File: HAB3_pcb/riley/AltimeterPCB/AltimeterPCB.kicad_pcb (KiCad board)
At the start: 2 copper layers, 4 parts, among them J1 Conn_01x04_Female, J2 Conn_02x01, U1 MS560702BA03-00

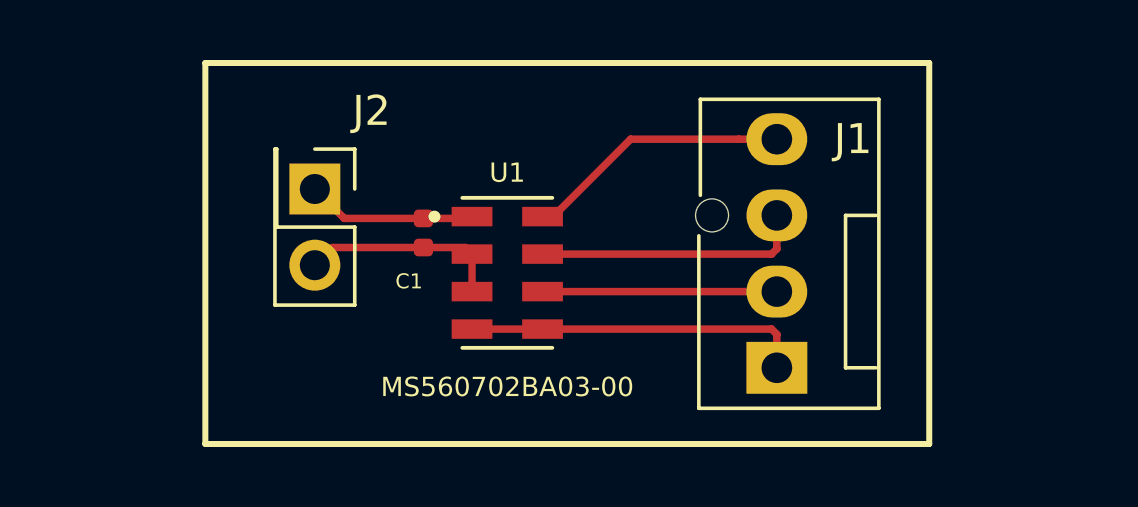
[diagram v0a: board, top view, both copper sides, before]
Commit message: updated labels on riley's pcb
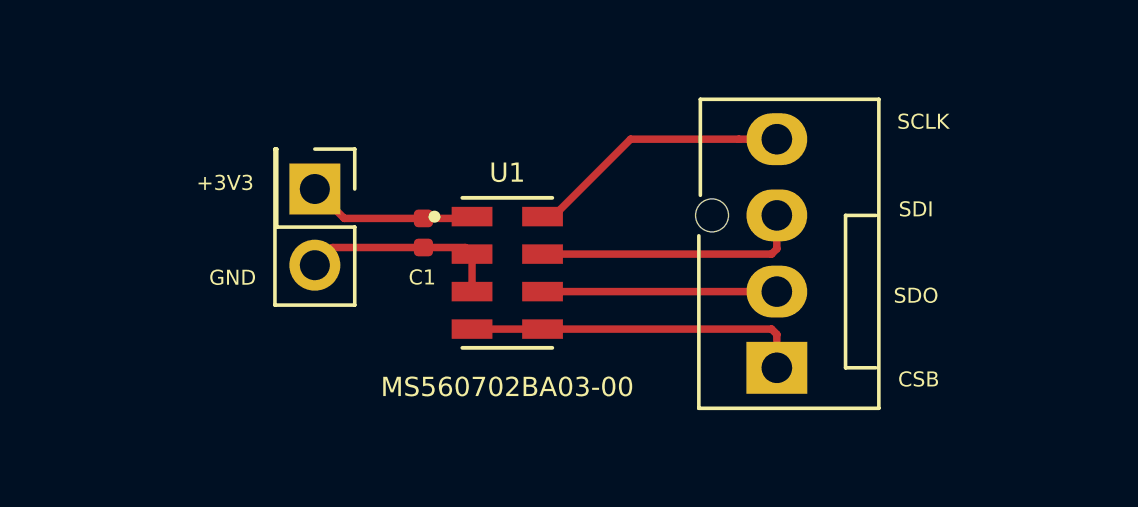
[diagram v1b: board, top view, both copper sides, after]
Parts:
- ?: renamed from J1; value Conn_01x04_Female -> (none)
- ?: renamed from J2; value Conn_02x01 -> (none)
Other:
- copper layers 2 -> 4
- board text added: "+3V3"
- board text added: "CSB"
- board text added: "GND"
- board text added: "SCLK"
- board text added: "SDI"
- board text added: "SDO"
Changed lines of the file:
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@@
   (layers
     (0 F.Cu signal)
+    (1 In1.Cu power)
+    (2 In2.Cu power)
     (31 B.Cu signal)
     (32 B.Adhes user)
@@
     (descr "4-pin CPU fan Through hole pin header, e.g. for Wieson part number 2366C888-007 Molex 47053-1000, Foxconn HF27040-M1, Tyco 1470947-1 or equivalent, see http://www.formfactors.org/developer%5Cspecs%5Crev1_2_public.pdf")
     (tags "pin header 4-pin CPU fan")
-    (fp_text reference J1 (at 7.62 2.54) (layer F.SilkS)
-      (effects (font (size 1 1) (thickness 0.15)))
-    )
-    (fp_text value Conn_01x04_Female (at 3.83 4.21 90) (layer F.Fab)
+    (fp_text reference "" (at 5.91 2.06) (layer F.SilkS) hide
+      (effects (font (size 1 1) (thickness 0.15)))
+    )
+    (fp_text value "" (at 3.83 4.21 90) (layer F.Fab) hide
       (effects (font (size 0.5 0.5) (thickness 0.125)))
     )
@@
     (tags capacitor)
     (attr smd)
-    (fp_text reference C1 (at 1.615 0.48) (layer F.SilkS)
+    (fp_text reference C1 (at 1.485 0.04) (layer F.SilkS)
       (effects (font (size 0.5 0.5) (thickness 0.125)))
     )
@@
     (descr "Through hole straight pin header, 2x01, 2.54mm pitch, double rows")
     (tags "Through hole pin header THT 2x01 2.54mm double row")
-    (fp_text reference J2 (at -2.6 -1.89) (layer F.SilkS)
-      (effects (font (size 1 1) (thickness 0.15)))
-    )
-    (fp_text value Conn_02x01 (at 1.25 2.57 270) (layer F.Fab)
+    (fp_text reference "" (at -2.6 -1.89) (layer F.SilkS) hide
+      (effects (font (size 1 1) (thickness 0.15)))
+    )
+    (fp_text value "" (at 1.25 2.57 270) (layer F.Fab)
       (effects (font (size 1 1) (thickness 0.15)))
     )
@@
     )
   )
-  (gr_line (start 116.84 109.22) (end 124.46 109.22) (layer F.SilkS) (width 0.2))
-  (gr_line (start 116.84 96.52) (end 116.84 109.22) (layer F.SilkS) (width 0.2))
-  (gr_line (start 124.46 96.52) (end 116.84 96.52) (layer F.SilkS) (width 0.2))
-  (gr_line (start 119.38 96.52) (end 140.97 96.52) (layer F.SilkS) (width 0.2))
-  (gr_line (start 140.97 109.22) (end 119.38 109.22) (layer F.SilkS) (width 0.2))
-  (gr_line (start 140.97 96.52) (end 140.97 109.22) (layer F.SilkS) (width 0.2))
+  (gr_text GND (at 117.75 103.68) (layer F.SilkS)
+    (effects (font (size 0.5 0.5) (thickness 0.125)))
+  )
+  (gr_text +3V3 (at 117.5 100.52) (layer F.SilkS)
+    (effects (font (size 0.5 0.5) (thickness 0.075)))
+  )
+  (gr_text CSB (at 140.62 107.07) (layer F.SilkS)
+    (effects (font (size 0.5 0.5) (thickness 0.125)))
+  )
+  (gr_text SDO (at 140.53 104.28) (layer F.SilkS)
+    (effects (font (size 0.5 0.5) (thickness 0.125)))
+  )
+  (gr_text SDI (at 140.53 101.4) (layer F.SilkS)
+    (effects (font (size 0.5 0.5) (thickness 0.125)))
+  )
+  (gr_text SCLK (at 140.77 98.48) (layer F.SilkS)
+    (effects (font (size 0.5 0.5) (thickness 0.125)))
+  )
   (segment (start 125.67 101.7) (end 125.73 101.64) (width 0.25) (layer F.Cu) (net 1) (status 30))
   (segment (start 124.11 101.7) (end 125.67 101.7) (width 0.25) (layer F.Cu) (net 1) (status 30))

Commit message: changed fonts to be thicker, 0402 -> 0603_hand_solder
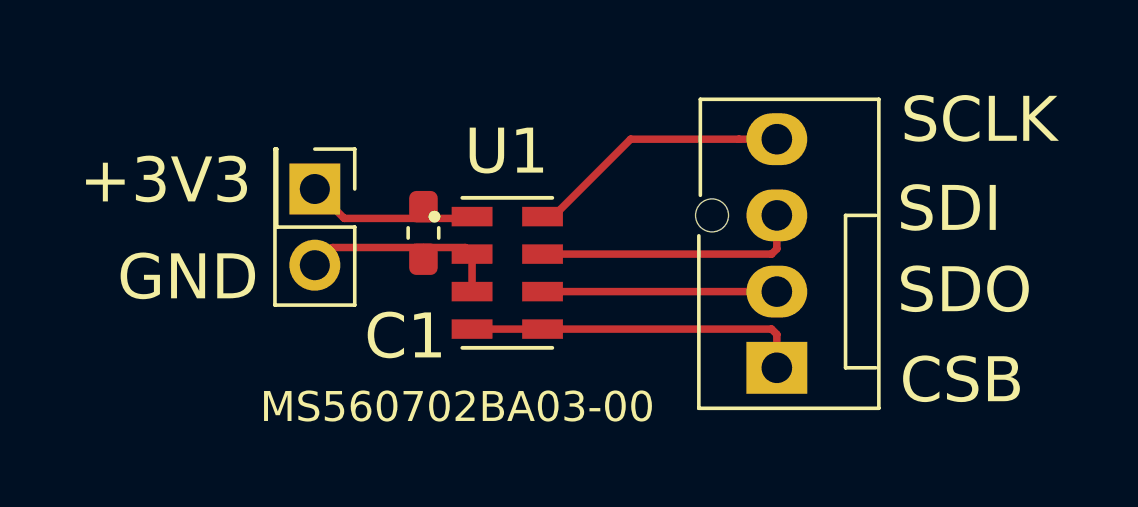
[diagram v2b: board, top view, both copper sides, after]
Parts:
- C1: value 100nF -> (none); footprint Capacitor_SMD:C_0402_1005Metric -> Capacitor_SMD:C_0603_1608Metric_Pad1.05x0.95mm_HandSolder
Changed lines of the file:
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@@
-(kicad_pcb (version 20171130) (host pcbnew "(5.0.0)")
+(kicad_pcb (version 20171130) (host pcbnew 5.0.1-33cea8e~68~ubuntu18.04.1)
   (general
     (thickness 1.6)
@@
     (pad_drill 0.6)
     (pad_to_mask_clearance 0)
+    (solder_mask_min_width 0.25)
     (aux_axis_origin 0 0)
     (visible_elements 7FFFFFFF)
@@
     (add_net /SDO)
     (add_net GND)
+  )
+  (module Capacitor_SMD:C_0603_1608Metric_Pad1.05x0.95mm_HandSolder (layer F.Cu)
+    (at 124.11 102.185 270)
+    (descr "Capacitor SMD 0603 (1608 Metric), square (rectangular) end terminal, IPC_7351 nominal with elongated pad for handsoldering. (Body size source: http://www.tortai-tech.com/upload/download/2011102023233369053.pdf), generated with kicad-footprint-generator")
+    (tags "capacitor handsolder")
+    (attr smd)
+    (fp_text reference C1 (at 3.455 0.6) (layer F.SilkS)
+      (effects (font (size 1.5 1.5) (thickness 0.375)))
+    )
+    (fp_text value "" (at -6.285 -0.02 270) (layer F.Fab) hide
+      (effects (font (size 1 1) (thickness 0.15)))
+    )
+    (fp_text user %R (at 0 0 270) (layer F.Fab)
+      (effects (font (size 0.4 0.4) (thickness 0.06)))
+    )
+    (fp_line (start 1.65 0.73) (end -1.65 0.73) (layer F.CrtYd) (width 0.05))
+    (fp_line (start 1.65 -0.73) (end 1.65 0.73) (layer F.CrtYd) (width 0.05))
+    (fp_line (start -1.65 -0.73) (end 1.65 -0.73) (layer F.CrtYd) (width 0.05))
+    (fp_line (start -1.65 0.73) (end -1.65 -0.73) (layer F.CrtYd) (width 0.05))
+    (fp_line (start -0.171267 0.51) (end 0.171267 0.51) (layer F.SilkS) (width 0.12))
+    (fp_line (start -0.171267 -0.51) (end 0.171267 -0.51) (layer F.SilkS) (width 0.12))
+    (fp_line (start 0.8 0.4) (end -0.8 0.4) (layer F.Fab) (width 0.1))
+    (fp_line (start 0.8 -0.4) (end 0.8 0.4) (layer F.Fab) (width 0.1))
+    (fp_line (start -0.8 -0.4) (end 0.8 -0.4) (layer F.Fab) (width 0.1))
+    (fp_line (start -0.8 0.4) (end -0.8 -0.4) (layer F.Fab) (width 0.1))
+    (pad 2 smd roundrect (at 0.875 0 270) (size 1.05 0.95) (layers F.Cu F.Paste F.Mask) (roundrect_rratio 0.25)
+      (net 2 GND))
+    (pad 1 smd roundrect (at -0.875 0 270) (size 1.05 0.95) (layers F.Cu F.Paste F.Mask) (roundrect_rratio 0.25)
+      (net 1 +3V3))
+    (model ${KISYS3DMOD}/Capacitor_SMD.3dshapes/C_0603_1608Metric.wrl
+      (at (xyz 0 0 0))
+      (scale (xyz 1 1 1))
+      (rotate (xyz 0 0 0))
+    )
   )
   (module Connector:FanPinHeader_1x04_P2.54mm_Vertical (layer F.Cu)
@@
     (at 126.905 103.515)
     (attr smd)
-    (fp_text reference U1 (at 0 -3.3333) (layer F.SilkS)
-      (effects (font (size 0.641134 0.641134) (thickness 0.05)))
-    )
-    (fp_text value MS560702BA03-00 (at 0 3.81) (layer F.SilkS)
-      (effects (font (size 0.641908 0.641908) (thickness 0.05)))
+    (fp_text reference U1 (at -0.025 -4.035) (layer F.SilkS)
+      (effects (font (size 1.5 1.5) (thickness 0.375)))
+    )
+    (fp_text value MS560702BA03-00 (at -1.665 4.475) (layer F.SilkS)
+      (effects (font (size 1 1) (thickness 0.25)))
     )
     (fp_line (start -1.5 -2.5) (end -1.5 2.5) (layer Dwgs.User) (width 0.127))
@@
       (net 5 /SDI))
   )
-  (module Capacitor_SMD:C_0402_1005Metric (layer F.Cu)
-    (at 124.11 102.185 270)
-    (descr "Capacitor SMD 0402 (1005 Metric), square (rectangular) end terminal, IPC_7351 nominal, (Body size source: http://www.tortai-tech.com/upload/download/2011102023233369053.pdf), generated with kicad-footprint-generator")
-    (tags capacitor)
-    (attr smd)
-    (fp_text reference C1 (at 1.485 0.04) (layer F.SilkS)
-      (effects (font (size 0.5 0.5) (thickness 0.125)))
-    )
-    (fp_text value 100nF (at -1.395 0.84) (layer F.Fab)
-      (effects (font (size 0.25 0.25) (thickness 0.0625)))
-    )
-    (fp_line (start -0.5 0.25) (end -0.5 -0.25) (layer F.Fab) (width 0.1))
-    (fp_line (start -0.5 -0.25) (end 0.5 -0.25) (layer F.Fab) (width 0.1))
-    (fp_line (start 0.5 -0.25) (end 0.5 0.25) (layer F.Fab) (width 0.1))
-    (fp_line (start 0.5 0.25) (end -0.5 0.25) (layer F.Fab) (width 0.1))
-    (fp_line (start -0.93 0.47) (end -0.93 -0.47) (layer F.CrtYd) (width 0.05))
-    (fp_line (start -0.93 -0.47) (end 0.93 -0.47) (layer F.CrtYd) (width 0.05))
-    (fp_line (start 0.93 -0.47) (end 0.93 0.47) (layer F.CrtYd) (width 0.05))
-    (fp_line (start 0.93 0.47) (end -0.93 0.47) (layer F.CrtYd) (width 0.05))
-    (fp_text user %R (at 0 0 270) (layer F.Fab)
-      (effects (font (size 0.25 0.25) (thickness 0.04)))
-    )
-    (pad 1 smd roundrect (at -0.485 0 270) (size 0.59 0.64) (layers F.Cu F.Paste F.Mask) (roundrect_rratio 0.25)
-      (net 1 +3V3))
-    (pad 2 smd roundrect (at 0.485 0 270) (size 0.59 0.64) (layers F.Cu F.Paste F.Mask) (roundrect_rratio 0.25)
-      (net 2 GND))
-    (model ${KISYS3DMOD}/Capacitor_SMD.3dshapes/C_0402_1005Metric.wrl
-      (at (xyz 0 0 0))
-      (scale (xyz 1 1 1))
-      (rotate (xyz 0 0 0))
-    )
-  )
   (module Connector_PinHeader_2.54mm:PinHeader_2x01_P2.54mm_Vertical (layer F.Cu)
     (at 120.49 100.72 270)
@@
     )
   )
-  (gr_text GND (at 117.75 103.68) (layer F.SilkS)
-    (effects (font (size 0.5 0.5) (thickness 0.125)))
-  )
-  (gr_text +3V3 (at 117.5 100.52) (layer F.SilkS)
-    (effects (font (size 0.5 0.5) (thickness 0.075)))
-  )
-  (gr_text CSB (at 140.62 107.07) (layer F.SilkS)
-    (effects (font (size 0.5 0.5) (thickness 0.125)))
-  )
-  (gr_text SDO (at 140.53 104.28) (layer F.SilkS)
-    (effects (font (size 0.5 0.5) (thickness 0.125)))
-  )
-  (gr_text SDI (at 140.53 101.4) (layer F.SilkS)
-    (effects (font (size 0.5 0.5) (thickness 0.125)))
-  )
-  (gr_text SCLK (at 140.77 98.48) (layer F.SilkS)
-    (effects (font (size 0.5 0.5) (thickness 0.125)))
+  (gr_text GND (at 116.26 103.67) (layer F.SilkS)
+    (effects (font (size 1.5 1.5) (thickness 0.375)))
+  )
+  (gr_text +3V3 (at 115.52 100.44) (layer F.SilkS)
+    (effects (font (size 1.5 1.5) (thickness 0.375)))
+  )
+  (gr_text CSB (at 142.06 107.1) (layer F.SilkS)
+    (effects (font (size 1.5 1.5) (thickness 0.375)))
+  )
+  (gr_text SDO (at 142.15 104.1) (layer F.SilkS)
+    (effects (font (size 1.5 1.5) (thickness 0.375)))
+  )
+  (gr_text SDI (at 141.64 101.39) (layer F.SilkS)
+    (effects (font (size 1.5 1.5) (thickness 0.375)))
+  )
+  (gr_text SCLK (at 142.63 98.42) (layer F.SilkS)
+    (effects (font (size 1.5 1.5) (thickness 0.375)))
   )
   (segment (start 125.67 101.7) (end 125.73 101.64) (width 0.25) (layer F.Cu) (net 1) (status 30))
